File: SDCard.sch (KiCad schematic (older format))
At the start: 1 part

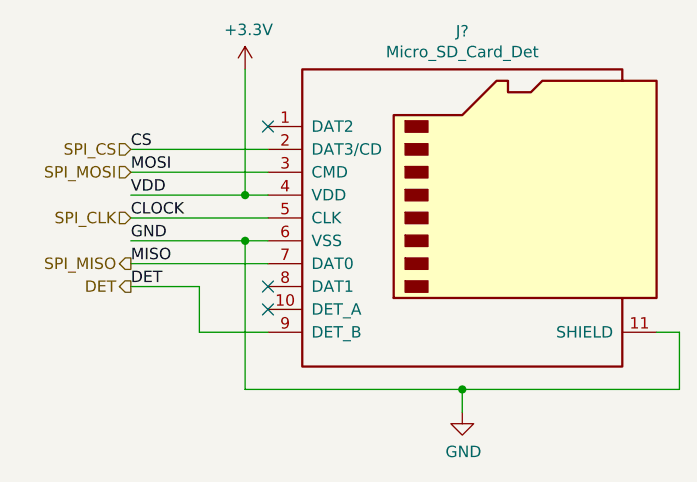
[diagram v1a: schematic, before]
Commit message: Initial layout of the Telemtry board.
The ethernet interface needs more work.
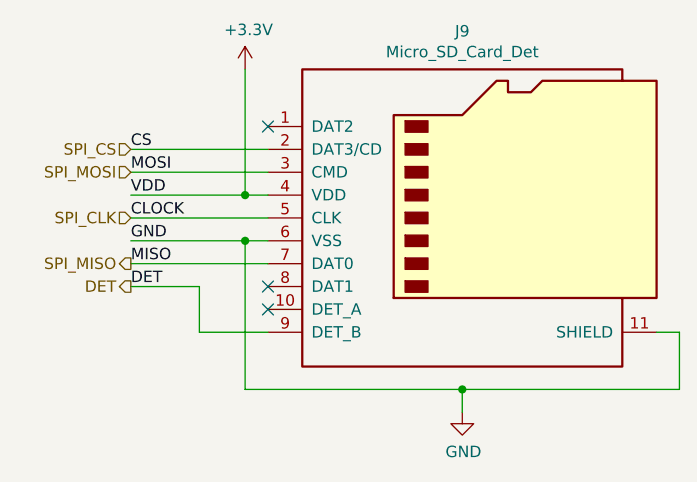
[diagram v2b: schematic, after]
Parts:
- gave numbers to parts that had none: 1
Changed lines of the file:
@@
 	4550 3600 3950 3600
 $Comp
-L Connector:Micro_SD_Card_Det J?
+L Connector:Micro_SD_Card_Det J9
 U 1 1 5F718A2C
 P 5450 3900
-F 0 "J?" H 5400 4717 50  0000 C CNN
+F 0 "J9" H 5400 4717 50  0000 C CNN
 F 1 "Micro_SD_Card_Det" H 5400 4626 50  0000 C CNN
 F 2 "Connector_Card:microSD_HC_Hirose_DM3AT-SF-PEJM5" H 7500 4600 50  0001 C CNN
@@
 P 5400 4750
 AR Path="/5F718A32" Ref="#PWR?"  Part="1"
-AR Path="/5F71644D/5F718A32" Ref="#PWR?"  Part="1"
-F 0 "#PWR?" H 5400 4500 50  0001 C CNN
+AR Path="/5F71644D/5F718A32" Ref="#PWR0147"  Part="1"
+F 0 "#PWR0147" H 5400 4500 50  0001 C CNN
 F 1 "GND" H 5405 4577 50  0000 C CNN
 F 2 "" H 5400 4750 50  0001 C CNN
@@
 	4450 3800 3950 3800
 $Comp
-L power:+3.3V #PWR?
+L power:+3.3V #PWR0148
 U 1 1 5F718A3D
 P 4450 3250
-F 0 "#PWR?" H 4450 3100 50  0001 C CNN
+F 0 "#PWR0148" H 4450 3100 50  0001 C CNN
 F 1 "+3.3V" H 4465 3423 50  0000 C CNN
 F 2 "" H 4450 3250 50  0001 C CNN

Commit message: Lay out the Telemetry board.
This is the initial draft of the Telemetry board layout. A few
debugging pins changed (on the SD card) for easier routing.

There is still some uncertainty with regard to the routing of the
Ethernet traces. According to my calculations, the differential
impedence between the RX+/- traces and the TX+/- traces is around
150R, which is 50% higher than one source was recommending. I am
uncertain how to reduce this though, and I am unclear as to how
much this will affect performance, especially when the traces
cover such a short distance.
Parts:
- J9: symbol Connector:Micro_SD_Card_Det -> Telemetry-Primary-rescue:Micro_SD_Card_Det-Connector
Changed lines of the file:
@@
 	4550 3600 3950 3600
 $Comp
-L Connector:Micro_SD_Card_Det J9
+L Telemetry-Primary-rescue:Micro_SD_Card_Det-Connector J9
 U 1 1 5F718A2C
 P 5450 3900
